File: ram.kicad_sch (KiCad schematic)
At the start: 87 parts, among them J1 DIN41612_01x32_A, J2 DIN41612_01x32_B, J3 DIN41612_01x32_C

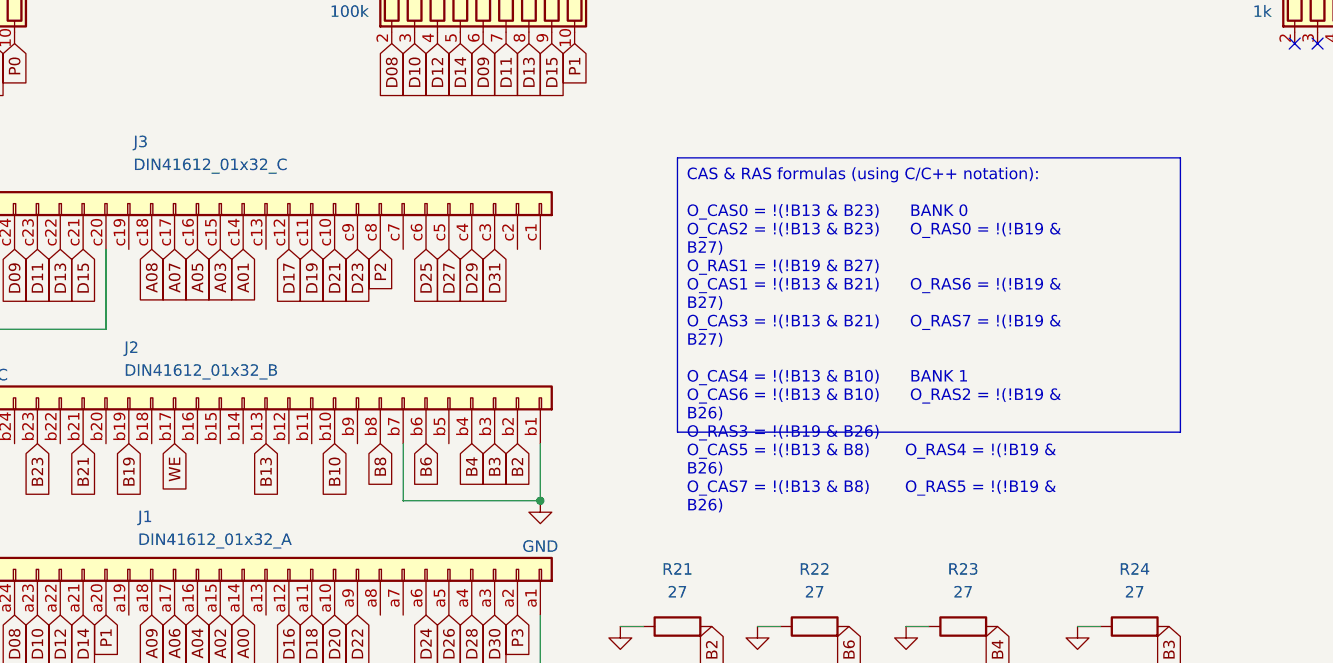
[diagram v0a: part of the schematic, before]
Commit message: Fixed WE pin (it's on B16 not B17)
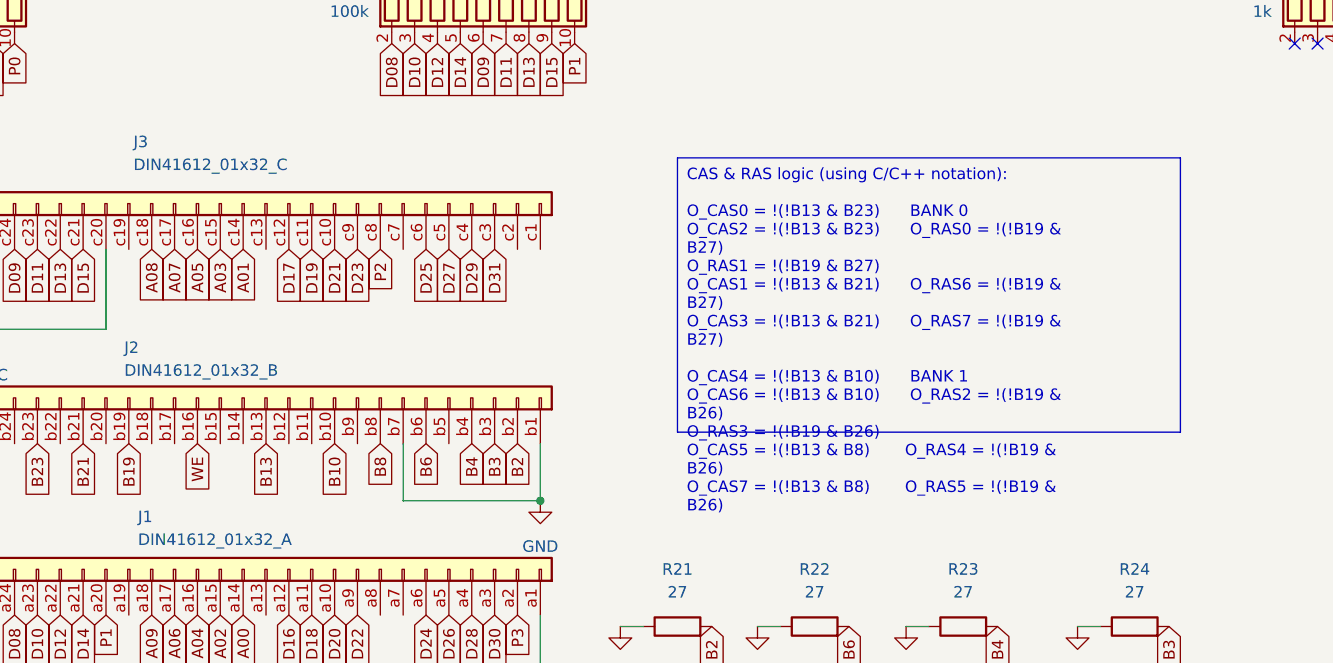
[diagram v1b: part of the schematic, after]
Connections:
- net WE: now also J2.b16 (Pin_b16); no longer J2.b17 (Pin_b17)
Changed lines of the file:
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@@
 		)
 	)
-	(text_box "CAS & RAS formulas (using C/C++ notation):\n\nO_CAS0 = !(!B13 & B23)      BANK 0\nO_CAS2 = !(!B13 & B23)      O_RAS0 = !(!B19 & B27)\n                            O_RAS1 = !(!B19 & B27)\nO_CAS1 = !(!B13 & B21)      O_RAS6 = !(!B19 & B27)\nO_CAS3 = !(!B13 & B21)      O_RAS7 = !(!B19 & B27)\n\nO_CAS4 = !(!B13 & B10)      BANK 1\nO_CAS6 = !(!B13 & B10)      O_RAS2 = !(!B19 & B26)\n                            O_RAS3 = !(!B19 & B26)\nO_CAS5 = !(!B13 & B8)       O_RAS4 = !(!B19 & B26)\nO_CAS7 = !(!B13 & B8)       O_RAS5 = !(!B19 & B26)\n\n\n"
+	(text_box "CAS & RAS logic (using C/C++ notation):\n\nO_CAS0 = !(!B13 & B23)      BANK 0\nO_CAS2 = !(!B13 & B23)      O_RAS0 = !(!B19 & B27)\n                            O_RAS1 = !(!B19 & B27)\nO_CAS1 = !(!B13 & B21)      O_RAS6 = !(!B19 & B27)\nO_CAS3 = !(!B13 & B21)      O_RAS7 = !(!B19 & B27)\n\nO_CAS4 = !(!B13 & B10)      BANK 1\nO_CAS6 = !(!B13 & B10)      O_RAS2 = !(!B19 & B26)\n                            O_RAS3 = !(!B19 & B26)\nO_CAS5 = !(!B13 & B8)       O_RAS4 = !(!B19 & B26)\nO_CAS7 = !(!B13 & B8)       O_RAS5 = !(!B19 & B26)\n\n\n"
 		(exclude_from_sim no)
 		(at 113.03 224.79 0)
@@
 		)
 	)
+	(global_label "WE"
+		(shape input)
+		(at 59.69 256.54 270)
+		(fields_autoplaced yes)
+		(effects
+			(font
+				(size 1.27 1.27)
+			)
+			(justify right)
+		)
+		(property "Intersheetrefs" "${INTERSHEET_REFS}"
+			(at 59.69 263.2142 90)
+			(effects
+				(font
+					(size 1.27 1.27)
+				)
+				(justify right)
+				(hide yes)
+			)
+		)
+	)
 	(global_label "D23"
 		(shape input)
@@
 			(effects
 				(font
-					(size 1.27 1.27)
-				)
-				(justify right)
-				(hide yes)
-			)
-		)
-	)
-	(global_label "WE"
-		(shape input)
-		(at 57.15 256.54 270)
-		(fields_autoplaced yes)
-		(effects
-			(font
-				(size 1.27 1.27)
-			)
-			(justify right)
-		)
-		(property "Intersheetrefs" "${INTERSHEET_REFS}"
-			(at 57.15 263.2142 90)
-			(effects
-				(font

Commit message: Identify the remaining connector pins
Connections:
- net A00: now also RN2.3 (R2)
- net A01: now also RN2.4 (R3)
- net A02: now also RN2.5 (R4)
- net A03: now also RN2.6 (R5)
- net A04: now also RN2.7 (R6)
- net A05: now also RN5.2 (R1)
- net A06: now also RN5.3 (R2)
- net A07: now also RN5.4 (R3)
- net A08: now also RN5.5 (R4)
- net A09: now also RN2.2 (R1)
- net GND: now also J1.a13 (Pin_a13), J1.a25 (Pin_a25), J1.a32 (Pin_a32), J1.a8 (Pin_a8), J2.b12 (Pin_b12), J2.b14 (Pin_b14), J2.b18 (Pin_b18), J2.b20 (Pin_b20), J2.b24 (Pin_b24), J2.b28 (Pin_b28), J2.b32 (Pin_b32), J3.c19 (Pin_c19), J3.c2 (Pin_c2), J3.c31 (Pin_c31), J3.c7 (Pin_c7)
- net P0: no longer J1.a2 (Pin_a2), J1.a20 (Pin_a20), J3.c8 (Pin_c8), RN12.10 (R9), RN13.10 (R9), RN14.10 (R9), SIM2.26 (QP), SIM2.29 (DP), SIM4.26 (QP), SIM4.29 (DP), SIM5.26 (QP), SIM5.29 (DP), SIM6.26 (QP), SIM6.29 (DP), SIM7.26 (QP), SIM7.29 (DP), SIM8.26 (QP), SIM8.29 (DP)
- net VCC: now also J1.a19 (Pin_a19), J1.a26 (Pin_a26), J1.a31 (Pin_a31), J1.a7 (Pin_a7), J2.b11 (Pin_b11), J2.b15 (Pin_b15), J2.b17 (Pin_b17), J2.b22 (Pin_b22), J2.b25 (Pin_b25), J2.b31 (Pin_b31), J2.b5 (Pin_b5), J2.b9 (Pin_b9), J3.c1 (Pin_c1), J3.c13 (Pin_c13), J3.c32 (Pin_c32)
- new net P1: J1.a20 (Pin_a20), RN12.10 (R9), SIM2.26 (QP), SIM2.29 (DP), SIM4.26 (QP), SIM4.29 (DP)
- new net P2: J3.c8 (Pin_c8), RN13.10 (R9), SIM5.26 (QP), SIM5.29 (DP), SIM7.26 (QP), SIM7.29 (DP)
- new net P3: J1.a2 (Pin_a2), RN14.10 (R9), SIM6.26 (QP), SIM6.29 (DP), SIM8.26 (QP), SIM8.29 (DP)
- no-connect marks 38 -> 30
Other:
- note added: "BANK 0"
- note added: "BANK 1"
- note added: "BYTE 0"
- note added: "BYTE 1"
- note added: "BYTE 2"
- note added: "BYTE 3"
- moved on the sheet: C1, C2, C21, C22, C23, C24, C25, C26, C3, C4, C6, C7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

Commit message: Fixed all CAS & RAS pins
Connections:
- net B10 is gone; now on net CAS2: J2.b10 (Pin_b10), U10.13 (4B), U12.13 (4B)
- net B21 is gone; now on net CAS1: J2.b21 (Pin_b21), U11.2 (1B), U9.2 (1B)
- net B23 is gone; now on net CAS0: J2.b23 (Pin_b23), U10.2 (1B), U12.2 (1B)
- net B26 is gone; now on net RAS1: J2.b26 (Pin_b26), U11.10 (3B), U11.5 (2B), U12.10 (3B), U12.5 (2B)
- net B27 is gone; now on net RAS0: J2.b27 (Pin_b27), U10.10 (3B), U10.5 (2B), U9.10 (3B), U9.5 (2B)
- net B8 is gone; now on net CAS3: J2.b8 (Pin_b8), U11.13 (4B), U9.13 (4B)
- net CAS0: no longer R6.2, SIM1.2 (~{CAS}), SIM1.28 (~{CASP})
- net CAS1: no longer R2.2, SIM2.2 (~{CAS}), SIM2.28 (~{CASP})
- net CAS2: no longer R16.1, SIM3.2 (~{CAS}), SIM3.28 (~{CASP})
- net CAS3: no longer R12.1, SIM4.2 (~{CAS}), SIM4.28 (~{CASP})
- net RAS0: no longer R5.2, SIM1.27 (~{RAS})
- net RAS1: no longer R1.2, SIM2.27 (~{RAS})
- net B13 renamed ~{CAS_OE}
- net B19 renamed ~{RAS_OE}
- net CAS4 renamed ~{CAS4}
- net CAS5 renamed ~{CAS5}
- net CAS6 renamed ~{CAS6}
- net CAS7 renamed ~{CAS7}
- net O_CAS0 renamed ~{O_CAS0}
- net O_CAS1 renamed ~{O_CAS1}
- net O_CAS2 renamed ~{O_CAS2}
- net O_CAS3 renamed ~{O_CAS3}
- net O_CAS4 renamed ~{O_CAS4}
- net O_CAS5 renamed ~{O_CAS5}
- net O_CAS6 renamed ~{O_CAS6}
- net O_CAS7 renamed ~{O_CAS7}
- net O_RAS0 renamed ~{O_RAS0}
- net O_RAS1 renamed ~{O_RAS1}
- net O_RAS2 renamed ~{O_RAS2}
- net O_RAS3 renamed ~{O_RAS3}
- net O_RAS4 renamed ~{O_RAS4}
- net O_RAS5 renamed ~{O_RAS5}
- net O_RAS6 renamed ~{O_RAS6}
- net O_RAS7 renamed ~{O_RAS7}
- net RAS2 renamed ~{RAS2}
- net RAS3 renamed ~{RAS3}
- net RAS4 renamed ~{RAS4}
- net RAS5 renamed ~{RAS5}
- net RAS6 renamed ~{RAS6}
- net RAS7 renamed ~{RAS7}
- net ~{B13} renamed CAS_OE
- net ~{B19} renamed RAS_OE
- new net ~{CAS0}: R6.2, SIM1.2 (~{CAS}), SIM1.28 (~{CASP})
- new net ~{CAS1}: R2.2, SIM2.2 (~{CAS}), SIM2.28 (~{CASP})
- new net ~{CAS2}: R16.1, SIM3.2 (~{CAS}), SIM3.28 (~{CASP})
- new net ~{CAS3}: R12.1, SIM4.2 (~{CAS}), SIM4.28 (~{CASP})
- new net ~{RAS0}: R5.2, SIM1.27 (~{RAS})
- new net ~{RAS1}: R1.2, SIM2.27 (~{RAS})
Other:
- moved on the sheet: R21, R22, R23, R24

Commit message: WIP: 8MB 72 pin SIMM to Altos 8MB RAM module
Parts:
- removed C1, C13, C17, C22, C23, C24, C25, C3, C4, C6, C7, C9: C, symbol Device:C_Polarized
- removed C10, C11, C12, C14, C15, C16, C18, C19, C20: C, symbol Device:C
- removed C21, C26, C8: 4.5n, symbol Device:C
- removed J1: DIN41612_01x32_A, symbol Connector:DIN41612_01x32_A
- removed J2: DIN41612_01x32_B, symbol chips:DIN41612_01x32_B
- removed J3: DIN41612_01x32_C, symbol chips:DIN41612_01x32_C
- removed R1, R10, R11, R12, R13, R14, R15, R16, R17, R18, R19, R2, R20, R21, R22, R23, R24, R3, R4, R5, R6, R7, R8, R9: 27, symbol Device:R
- removed RN1, RN10, RN3, RN4, RN6, RN7, RN8, RN9: 22, Resistor_THT:R_Array_SIP10, symbol Device:R_Pack05_SIP
- removed RN11, RN12, RN13, RN14: 100k, Resistor_THT:R_Array_SIP10, symbol Device:R_Network09
- removed RN2, RN5: 1k, Resistor_THT:R_Array_SIP10, symbol Device:R_Network09
- removed SIM1, SIM2, SIM3, SIM4, SIM5, SIM6, SIM7, SIM8: ~, symbol chips:SIMM_1X30_PIN
- removed U1, U2, U3, U4, U5, U6, U7, U8: ~, symbol chips:SN54AS1004A
- removed U10, U12, U9: ~, symbol chips:SN74AS1000A
- added C1: 0.1uF, Capacitor_SMD:C_1210_3225Metric, symbol Device:C
- added C3: C, Capacitor_SMD:C_1210_3225Metric, symbol Device:C
- added J1: ~, Sockets:DIN41612_R_3x32_Male_Horizontal_THT, symbol chips:DIN41612_03x32
- added U1, U3: 74AHCT1G00, Package_TO_SOT_SMD:SOT-23-5, symbol 74xGxx:74AHCT1G00
- added U13: ~, Sockets:SIM72, symbol chips:SIMM_1X72_PIN
- added U4: ~, Package_SO:TSSOP-8_3x3mm_P0.65mm, symbol chips:74AHCT3G04
- C2: value 4.5n -> 0.1uF; footprint (none) -> Capacitor_SMD:C_1210_3225Metric
- C5: footprint (none) -> Capacitor_SMD:C_1210_3225Metric
- U11: footprint (none) -> Package_SO:SSOP-14_5.3x6.2mm_P0.65mm
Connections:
- net ~{O_CAS3} is gone; now on net ~{CAS0}: U11.3 (1Y)
- net ~{O_CAS5} is gone; now on net ~{CAS2}: U11.11 (4Y)
- net ~{O_RAS3} is gone; now on net ~{CAS1}: U11.6 (2Y)
- net ~{O_RAS5} is gone; now on net ~{CAS3}: U11.8 (3Y)
- net A00: now also J1.a14 (Pin_a14), U13.12 (A00)
- net A01: now also J1.c14 (Pin_c14), U13.13 (A01)
- net A02: now also J1.a15 (Pin_a15), U13.14 (A02)
- net A03: now also J1.c15 (Pin_c15), U13.15 (A03)
- net A04: now also J1.a16 (Pin_a16), U13.16 (A04)
- net A05: now also J1.c16 (Pin_c16), U13.17 (A05)
- net A06: now also J1.a17 (Pin_a17), U13.18 (A06)
- net A07: now also J1.c17 (Pin_c17), U13.28 (A07)
- net A08: now also J1.c18 (Pin_c18), U13.31 (A08)
- net A09: now also J1.a18 (Pin_a18), U13.32 (A09)
- net CAS0: now also U11.2 (1B), J1.b23 (Pin_b23)
- net CAS1: now also U11.5 (2B), J1.b21 (Pin_b21); no longer U11.2 (1B)
- net CAS2: now also U11.13 (4B), J1.b10 (Pin_b10)
- net CAS3: now also U11.10 (3B), J1.b8 (Pin_b8); no longer U11.13 (4B)
- net CAS_OE: now also J1.b13 (Pin_b13), U4.6 (3A); no longer U11.1 (1A), U11.12 (4A)
- net D00: now also J1.a30 (Pin_a30), U13.2 (D00)
- net D01: now also J1.c30 (Pin_c30), U13.4 (D01)
- net D02: now also J1.a29 (Pin_a29), U13.6 (D02)
- net D03: now also J1.c29 (Pin_c29), U13.8 (D03)
- net D04: now also J1.a28 (Pin_a28), U13.20 (D04)
- net D05: now also J1.c28 (Pin_c28), U13.22 (D05)
- net D06: now also J1.a27 (Pin_a27), U13.24 (D06)
- net D07: now also J1.c27 (Pin_c27), U13.26 (D07)
- net D08: now also J1.a24 (Pin_a24), U13.49 (D08)
- net D09: now also J1.c24 (Pin_c24), U13.51 (D09)
- net D10: now also J1.a23 (Pin_a23), U13.53 (D10)
- net D11: now also J1.c23 (Pin_c23), U13.55 (D11)
- net D12: now also J1.a22 (Pin_a22), U13.57 (D12)
- net D13: now also J1.c22 (Pin_c22), U13.61 (D13)
- net D14: now also J1.a21 (Pin_a21), U13.63 (D14)
- net D15: now also J1.c21 (Pin_c21), U13.65 (D15)
- net D16: now also J1.a12 (Pin_a12), U13.3 (D16)
- net D17: now also J1.c12 (Pin_c12), U13.5 (D17)
- net D18: now also J1.a11 (Pin_a11), U13.7 (D18)
- net D19: now also J1.c11 (Pin_c11), U13.9 (D19)
- net D20: now also J1.a10 (Pin_a10), U13.21 (D20)
- net D21: now also J1.c10 (Pin_c10), U13.23 (D21)
- net D22: now also J1.a9 (Pin_a9), U13.25 (D22)
- net D23: now also J1.c9 (Pin_c9), U13.27 (D23)
- net D24: now also J1.a6 (Pin_a6), U13.50 (D24)
- net D25: now also J1.c6 (Pin_c6), U13.52 (D25)
- net D26: now also J1.a5 (Pin_a5), U13.54 (D26)
- net D27: now also J1.c5 (Pin_c5), U13.56 (D27)
- net D28: now also J1.a4 (Pin_a4), U13.58 (D28)
- net D29: now also J1.c4 (Pin_c4), U13.60 (D29)
- net D30: now also J1.a3 (Pin_a3), U13.62 (D30)
- net D31: now also J1.c3 (Pin_c3), U13.64 (D31)
- net GND: now also C1.1, C3.1, J1.a1 (Pin_a1), J1.a13 (Pin_a13), J1.a25 (Pin_a25), J1.a32 (Pin_a32), J1.a8 (Pin_a8), J1.b1 (Pin_b1), J1.b12 (Pin_b12), J1.b14 (Pin_b14), J1.b18 (Pin_b18), J1.b2 (Pin_b2), J1.b20 (Pin_b20), J1.b24 (Pin_b24), J1.b28 (Pin_b28), J1.b3 (Pin_b3), J1.b32 (Pin_b32), J1.b4 (Pin_b4), J1.b6 (Pin_b6), J1.b7 (Pin_b7), J1.c19 (Pin_c19), J1.c2 (Pin_c2), J1.c31 (Pin_c31), J1.c7 (Pin_c7), U1.3 (GND), U13.1 (GND), U13.39 (GND), U13.72 (GND), U3.3 (GND), U4.4 (GND)
- net P0: now also J1.c26 (Pin_c26), U13.36 (P00)
- net P1: now also J1.a20 (Pin_a20), U13.37 (P01)
- net P2: now also J1.c8 (Pin_c8), U13.35 (P02)
- net P3: now also J1.a2 (Pin_a2), U13.38 (P03)
- net RAS0: now also J1.b27 (Pin_b27), U1.2
- net RAS1: now also J1.b26 (Pin_b26), U3.2; no longer U11.10 (3B), U11.5 (2B)
- net RAS_OE: now also J1.b19 (Pin_b19), U4.3 (2A); no longer U11.4 (2A), U11.9 (3A)
- net VCC: now also C3.2, J1.a19 (Pin_a19), J1.a26 (Pin_a26), J1.a31 (Pin_a31), J1.a7 (Pin_a7), J1.b11 (Pin_b11), J1.b15 (Pin_b15), J1.b17 (Pin_b17), J1.b22 (Pin_b22), J1.b25 (Pin_b25), J1.b31 (Pin_b31), J1.b5 (Pin_b5), J1.b9 (Pin_b9), J1.c1 (Pin_c1), J1.c13 (Pin_c13), J1.c20 (Pin_c20), J1.c25 (Pin_c25), J1.c32 (Pin_c32), U13.10 (VCC), U13.30 (VCC), U13.59 (VCC), U4.8 (VCC); no longer C2.2
- net WE: now also J1.b16 (Pin_b16), U4.1 (1A)
- net ~{CAS0}: now also U13.40 (~{CAS0})
- net ~{CAS1}: now also U13.43 (~{CAS1})
- net ~{CAS2}: now also U13.41 (~{CAS2})
- net ~{CAS3}: now also U13.42 (~{CAS3})
- net ~{CAS_OE}: now also U11.1 (1A), U11.12 (4A), U11.4 (2A), U11.9 (3A), U4.2 (3Y)
- net ~{RAS0}: now also U1.4, U13.34 (~{RAS2}), U13.44 (~{RAS0})
- net ~{RAS1}: now also U13.33 (~{RAS3}), U13.45 (~{RAS1}), U3.4
- net ~{RAS_OE}: now also U1.1, U3.1, U4.5 (2y)
- new net: C2.2, U3.5 (VCC)
- new net: C1.2, U1.5 (VCC)
- new net ~{WE}: U13.47 (~{WE}), U4.7 (1Y)
- no-connect marks 30 -> 2
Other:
- note removed: "BANK 0"
- note removed: "BANK 1"
- note removed: "BYTE 0"
- note removed: "BYTE 1"
- note removed: "BYTE 2"
- note removed: "BYTE 3"
- moved on the sheet: U11

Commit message: Add ICs descriptions
Cook first PCB iteration.
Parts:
- C3, C5: value C -> 0.1uF
- U1, U3: value 74AHCT1G00 -> SN74AHCT1G00DBVR
- U11: value ~ -> SN74AHCT00DR
- U4: value ~ -> 74AHCT3G04DC
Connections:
- net VCC: now also C1.2, C2.2, U1.5 (VCC), U3.5 (VCC)
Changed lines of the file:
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@@
 	)
 	(junction
+		(at 63.5 77.47)
+		(diameter 0)
+		(color 0 0 0 0)
+	)
+	(junction
 		(at 147.32 52.07)
 		(diameter 0)
@@
 	)
 	(junction
+		(at 113.03 74.93)
+		(diameter 0)
+		(color 0 0 0 0)
+	)
+	(junction
 		(at 144.78 245.11)
 		(diameter 0)
@@
 	(wire
 		(pts
-			(xy 110.49 74.93) (xy 114.3 74.93)
+			(xy 110.49 74.93) (xy 113.03 74.93)
 		)
 		(stroke
@@
 	(wire
 		(pts
-			(xy 60.96 77.47) (xy 64.77 77.47)
+			(xy 60.96 77.47) (xy 63.5 77.47)
 		)
 		(stroke
@@
 	(wire
 		(pts
+			(xy 63.5 77.47) (xy 64.77 77.47)
+		)
+		(stroke
+			(width 0)
+			(type default)
+		)
+	)
+	(wire
+		(pts
 			(xy 162.56 219.71) (xy 175.26 219.71)
 		)
@@
 	(wire
 		(pts
+			(xy 113.03 74.93) (xy 114.3 74.93)
+		)
+		(stroke
+			(width 0)
+			(type default)
+		)
+	)
+	(wire
+		(pts
 			(xy 129.54 198.12) (xy 142.24 198.12)
 		)
@@
 	)
 	(symbol
+		(lib_id "power:VCC")
+		(at 63.5 77.47 0)
+		(unit 1)
+		(exclude_from_sim no)
+		(in_bom yes)
+		(on_board yes)
+		(dnp no)
+		(fields_autoplaced yes)
+		(property "Reference" "#PWR08"
+			(at 63.5 81.28 0)
+			(effects
+				(font
+					(size 1.27 1.27)
+				)
+				(hide yes)
+			)
+		)
+		(property "Value" "VCC"
+			(at 63.5 72.39 0)
+			(effects
+				(font
+					(size 1.27 1.27)
+				)
+			)
+		)
+		(property "Footprint" ""
+			(at 63.5 77.47 0)
+			(effects
+				(font
+					(size 1.27 1.27)
+				)
+				(hide yes)
+			)
+		)
+		(property "Datasheet" ""
+			(at 63.5 77.47 0)
+			(effects
+				(font
+					(size 1.27 1.27)
+				)
+				(hide yes)
+			)
+		)
+		(property "Description" "Power symbol creates a global label with name \"VCC\""
+			(at 63.5 77.47 0)
+			(effects
+				(font
+					(size 1.27 1.27)
+				)
+				(hide yes)
+			)
+		)
+		(pin "1"
+		)
+		(instances
+			(project "ram"
+				(path "/97db9db7-dcb2-41a1-990d-fa9c47eb8645"
+					(reference "#PWR08")
+					(unit 1)
+				)
+			)
+		)
+	)
+	(symbol
 		(lib_id "power:GND")
 		(at 86.36 152.4 0)
@@
 			)
 		)
-		(property "Value" "~"
+		(property "Value" "74AHCT3G04DC"
 			(at 105.41 135.255 0)
 			(effects
@@
 			)
 		)
-		(property "Description" ""
+		(property "Description" "74AHCT3G04DC"
 			(at 99.06 120.65 0)
 			(effects
@@
 			)
 		)
-		(property "Value" "74AHCT1G00"
+		(property "Value" "SN74AHCT1G00DBVR"
 			(at 127 86.3914 0)
 			(effects
@@
 			)
 		)
-		(property "Value" "74AHCT1G00"
+		(property "Value" "SN74AHCT1G00DBVR"
 			(at 77.47 88.9314 0)
 			(effects
@@
 			)
 		)
-		(property "Value" "~"
+		(property "Value" "SN74AHCT00DR"
 			(at 55.88 127 0)
 			(effects
@@
 			)
 		)
-		(property "Description" ""
+		(property "Description" "SN74AHCT00DR"
 			(at 52.07 134.62 0)
 			(effects
@@
 			)
 		)
-		(property "Value" "C"
+		(property "Value" "0.1uF"
 			(at 55.88 113.03 90)
 			(effects
@@
 	(symbol
 		(lib_id "power:VCC")
+		(at 113.03 74.93 0)
+		(unit 1)
+		(exclude_from_sim no)
+		(in_bom yes)
+		(on_board yes)
+		(dnp no)
+		(fields_autoplaced yes)
+		(property "Reference" "#PWR011"
+			(at 113.03 78.74 0)
+			(effects
+				(font
+					(size 1.27 1.27)
+				)
+				(hide yes)
+			)
+		)
+		(property "Value" "VCC"
+			(at 113.03 69.85 0)
+			(effects
+				(font
+					(size 1.27 1.27)
+				)
+			)
+		)
+		(property "Footprint" ""
+			(at 113.03 74.93 0)
+			(effects
+				(font
+					(size 1.27 1.27)
+				)
+				(hide yes)
+			)
+		)
+		(property "Datasheet" ""
+			(at 113.03 74.93 0)
+			(effects
+				(font
+					(size 1.27 1.27)
+				)
+				(hide yes)
+			)
+		)
+		(property "Description" "Power symbol creates a global label with name \"VCC\""
+			(at 113.03 74.93 0)
+			(effects
+				(font
+					(size 1.27 1.27)
+				)
+				(hide yes)
+			)
+		)
+		(pin "1"
+		)
+		(instances
+			(project "ram"
+				(path "/97db9db7-dcb2-41a1-990d-fa9c47eb8645"
+					(reference "#PWR011")
+					(unit 1)
+				)
+			)
+		)
+	)
+	(symbol
+		(lib_id "power:VCC")
 		(at 107.95 241.3 0)
 		(unit 1)
@@
 			)
 		)
-		(property "Value" "C"
+		(property "Value" "0.1uF"
 			(at 90.17 147.32 90)
 			(effects
